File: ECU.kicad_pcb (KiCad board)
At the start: 4 copper layers, 134 x 123 mm, 117 parts, among them J1 Solenoid 0, J10 Thermocouple 3, J13 External SPI, J14 External UART, J15 External I2C, J16 Pressure Transducer 0, J17 Pressure Transducer 1, J18 Pressure Transducer 2, J19 Pressure Transducer 3, J2 Solenoid 1, J20 Pressure Transducer 4, J21 Pressure Transducer 5, J22 Power In, J3 Solenoid 2, J4 Solenoid 3, J5 Solenoid 4, J6 Solenoid 5, J7 Thermocouple 0, J8 Thermocouple 1, J9 Thermocouple 2, U1 Teensy4.1, U10 MAX31855, U11 MAX31855, U12 OPA357, U13 OPA357, U14 OPA357, U15 OPA357, U16 OPA357, U17 OPA357, U2 OPA357, U20 uA7805, U21 TLV2217, U3 OPA357, U4 OPA357, U5 OPA357, U6 OPA357, U7 OPA357, U8 MAX31855, U9 MAX31855

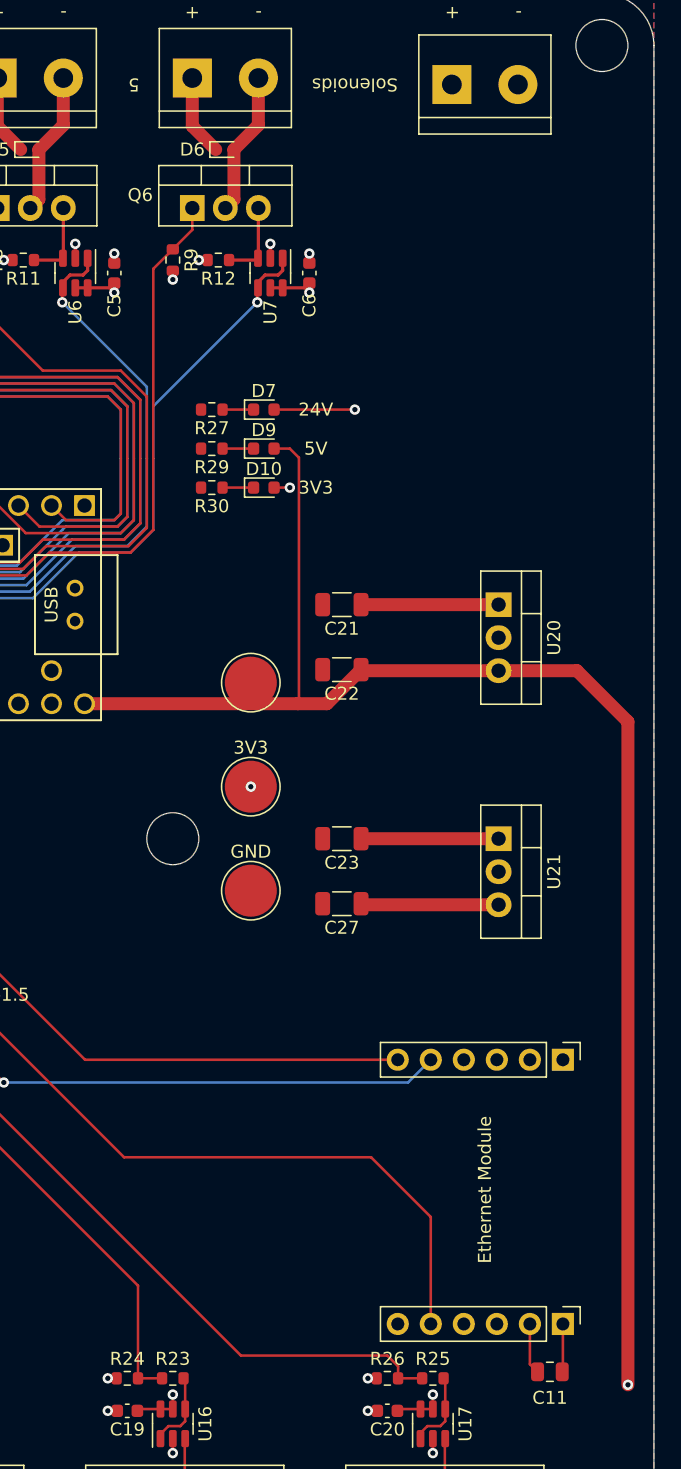
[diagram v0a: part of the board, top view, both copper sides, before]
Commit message: Integrate power switching & cutoff system
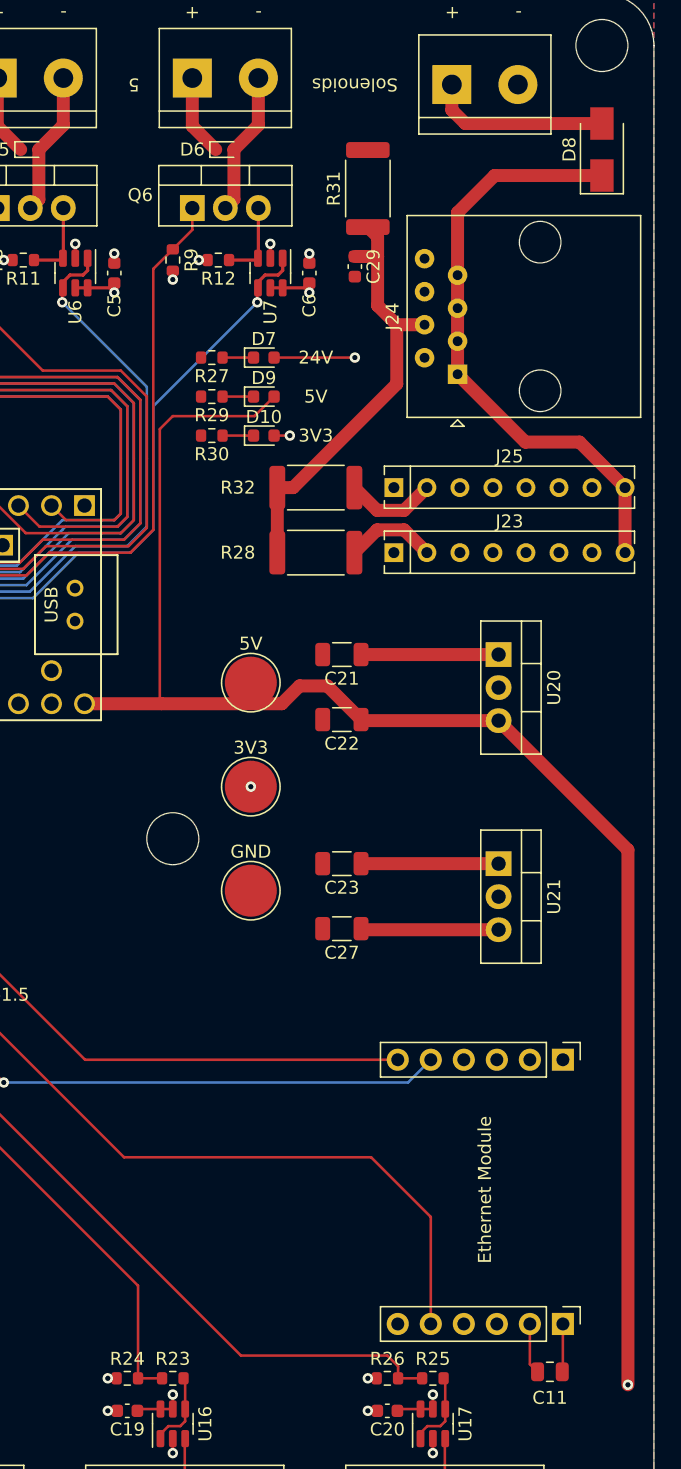
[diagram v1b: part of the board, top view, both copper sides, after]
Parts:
- added C29: 100nF, Capacitor_SMD:C_0603_1608Metric, F.Cu at (170.0, 44.0)
- added D8: ~, Diode_SMD:D_SMA, F.Cu at (189.0, 35.0)
- added J23: SSR SPST NC, Package_SIP:SIP-8_19x3mm_P2.54mm, F.Cu at (173.0, 66.0)
- added J24: RJ45, Connector_RJ:RJ45_Amphenol_54602-x08_Horizontal, F.Cu at (177.9, 52.3)
- added J25: SSR SPST NC, Package_SIP:SIP-8_19x3mm_P2.54mm, F.Cu at (173.0, 61.0)
- added R28: 1K, Resistor_SMD:R_2512_6332Metric, F.Cu at (167.0, 66.0)
- added R31: 1K, Resistor_SMD:R_2512_6332Metric, F.Cu at (171.0, 38.0)
- added R32: 1K, Resistor_SMD:R_2512_6332Metric, F.Cu at (167.0, 61.0)
- J22: value Power In -> BATT'
- moved D10 4.00 mm to (163.0, 57.0)
- moved D7 4.00 mm to (163.0, 51.0)
- moved D9 4.00 mm to (163.0, 54.0)
- moved R27 4.00 mm to (159.0, 51.0)
- moved R29 4.00 mm to (159.0, 54.0)
- moved R30 4.00 mm to (159.0, 57.0)
- moved C21 3.84 mm to (169.0, 73.8)
- moved C22 3.84 mm to (169.0, 78.8)
- moved U20 3.84 mm to (181.1, 73.8)
- moved C23 1.92 mm to (169.0, 89.9)
- moved C27 1.92 mm to (169.0, 94.9)
- moved U21 1.92 mm to (181.1, 89.9)
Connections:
- J22 pad 1: +24V -> Net-(J22-Pad1)
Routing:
- net VCC: track 0.00 -> 46.2 mm
- net Net-(C29-Pad1): track 0.00 -> 34.4 mm
- net Net-(J22-Pad1): track 0.00 -> 13.9 mm
- net Net-(J25-Pad2): track 0.00 -> 7.03 mm
- net Net-(J23-Pad2): track 0.00 -> 7.03 mm
- net +5V: track 140.1 -> 143.3 mm

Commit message: Add bypass path for PT frontend
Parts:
- added REF**: R_0402_1005Metric, Resistor_SMD:R_0402_1005Metric, F.Cu at (179.8, 133.0)
- added REF**: R_0402_1005Metric, Resistor_SMD:R_0402_1005Metric, F.Cu at (159.8, 133.0)
- added REF**: R_0402_1005Metric, Resistor_SMD:R_0402_1005Metric, F.Cu at (99.8, 133.0)
- added REF**: R_0402_1005Metric, Resistor_SMD:R_0402_1005Metric, F.Cu at (139.8, 133.0)
- added REF**: R_0402_1005Metric, Resistor_SMD:R_0402_1005Metric, F.Cu at (79.8, 133.0)
- added REF**: R_0402_1005Metric, Resistor_SMD:R_0402_1005Metric, F.Cu at (119.8, 133.0)
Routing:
- net Net-(R23-Pad1): track 6.01 -> 9.07 mm
- net Net-(R21-Pad1): track 6.06 -> 9.12 mm
- net Net-(J21-Pad2): track 5.87 -> 8.93 mm
- net Net-(J20-Pad2): track 5.87 -> 8.93 mm
- net Net-(J19-Pad2): track 5.87 -> 8.93 mm
- net Net-(R25-Pad1): track 6.06 -> 9.12 mm
- net Net-(R17-Pad1): track 6.01 -> 9.07 mm
- net Net-(R15-Pad1): track 6.06 -> 9.12 mm
- net Net-(J18-Pad2): track 5.87 -> 8.93 mm
- net Net-(J17-Pad2): track 5.87 -> 8.93 mm
- net Net-(J16-Pad2): track 5.87 -> 8.93 mm
- net Net-(R19-Pad1): track 6.01 -> 9.07 mm

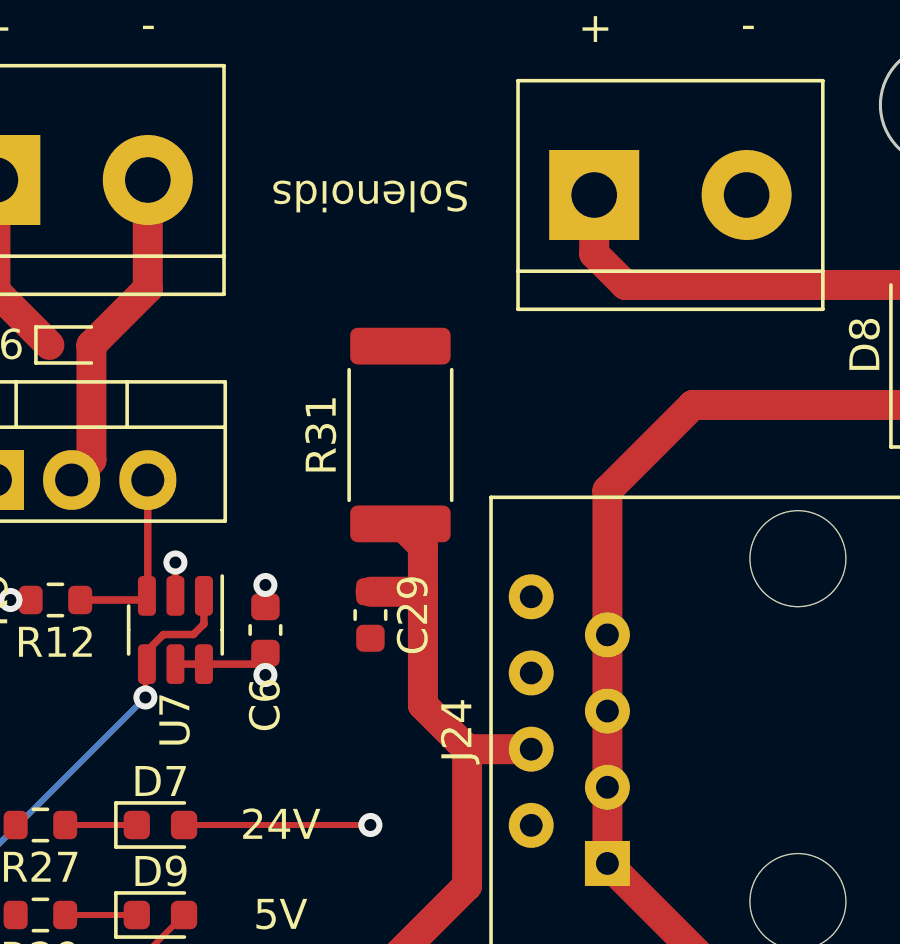
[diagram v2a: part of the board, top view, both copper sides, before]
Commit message: Add bypass path for cutoff system
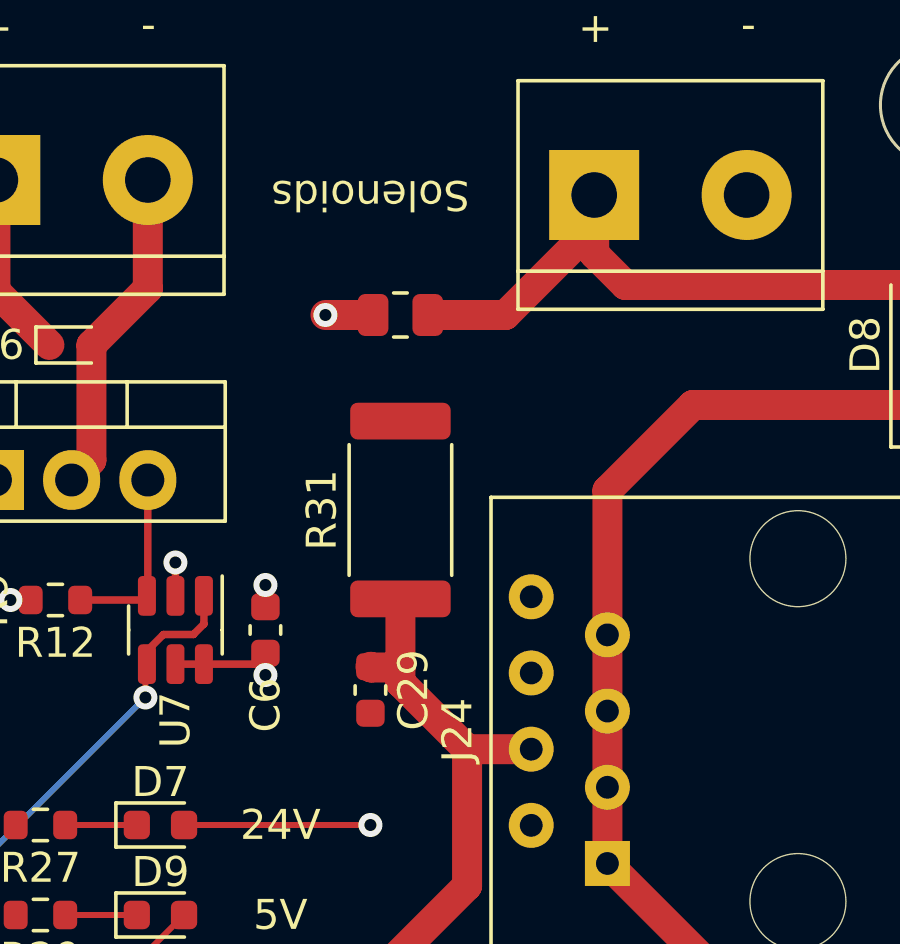
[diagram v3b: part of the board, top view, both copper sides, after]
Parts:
- added REF**: R_0805_2012Metric, Resistor_SMD:R_0805_2012Metric, F.Cu at (171.0, 34.0)
- moved C29 2.50 mm to (170.0, 46.5)
- moved R31 2.50 mm to (171.0, 40.5)
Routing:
- net Net-(J22-Pad1): track 13.9 -> 21.7 mm
- net Net-(C29-Pad1): track 34.4 -> 31.1 mm
- net +24V: track 64.8 -> 66.4 mm, vias 1 -> 2
